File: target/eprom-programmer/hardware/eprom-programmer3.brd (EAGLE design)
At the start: 68.6 x 61 mm, 42 parts, among them IC2 27C08032P6, Q1 BC557, Q2 BC557, Q3 BC557

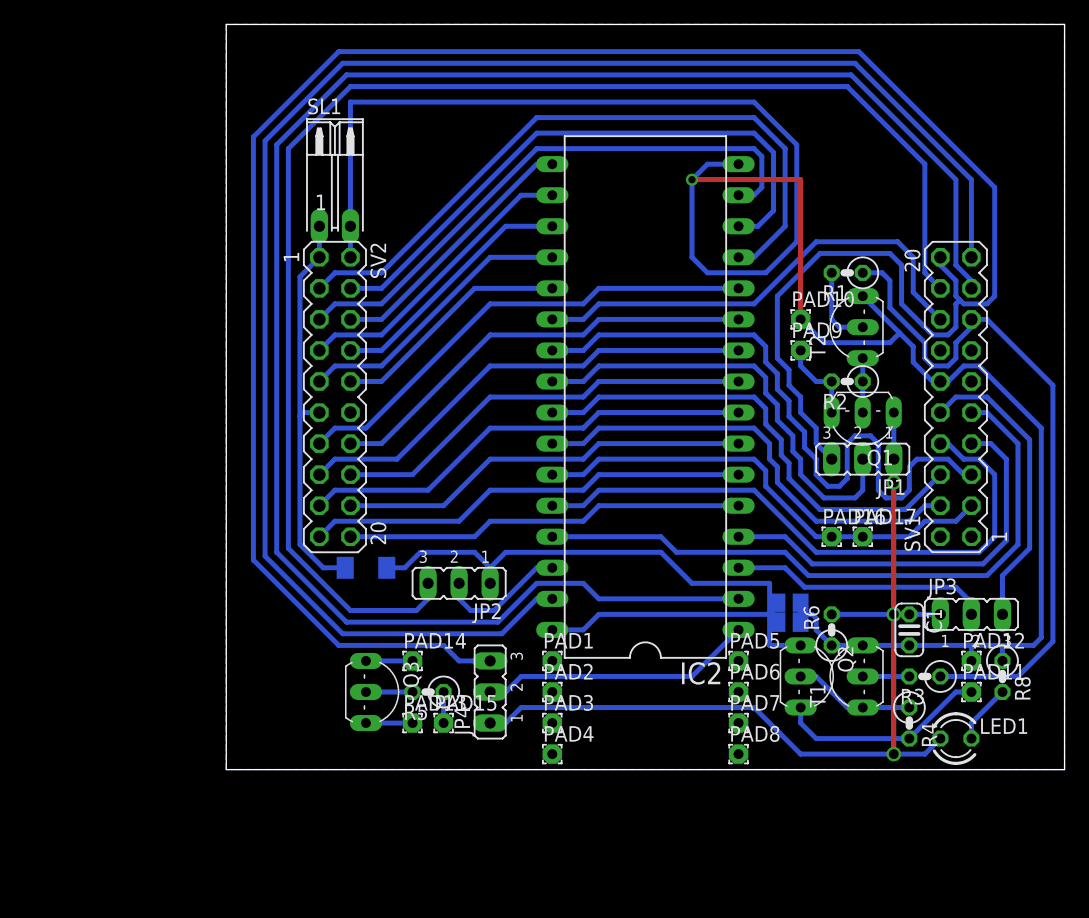
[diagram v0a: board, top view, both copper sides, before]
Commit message: eprom-programmer: hardware
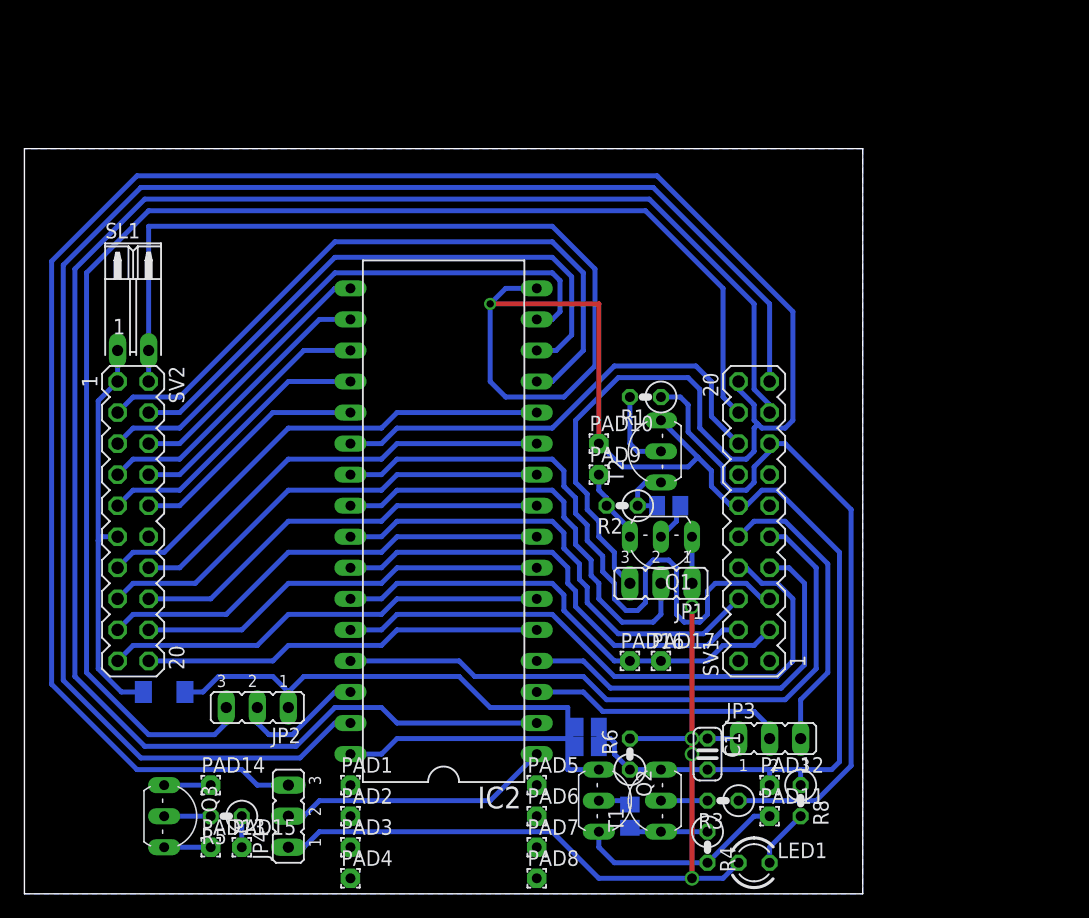
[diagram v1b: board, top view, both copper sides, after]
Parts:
- added R10, R9: 5k1, rcl:M0805
- moved R2 21.0 mm to (48.9, 31.8)
- moved PAD6 19.4 mm to (41.9, 6.35)
- moved D1 19.4 mm to (11.4, 16.5)
- moved JP4 19.4 mm to (21.6, 6.35)
- moved LED1 19.4 mm to (59.7, 2.54)
- moved PAD16 19.4 mm to (49.5, 19.1)
- moved PAD5 19.4 mm to (41.9, 8.89)
- moved PAD7 19.4 mm to (41.9, 3.81)
- moved PAD8 19.4 mm to (41.9, 1.27)
- moved Q3 19.4 mm to (12.7, 6.35)
- moved R1 19.4 mm to (50.8, 40.6)
- moved R5 19.4 mm to (16.5, 6.35)
- moved R6 19.4 mm to (49.5, 11.4)
- moved R8 19.4 mm to (63.5, 7.62)
- moved SV1 19.4 mm to (59.7, 30.5)
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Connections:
- new net N$11: Q1.B, R9.1
- new net N$14: Q2.B, R10.1
- net N$2: now also R10.2; no longer Q2.B
- net N$4: now also R9.2; no longer Q1.B
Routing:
- net N$2: track 9.94 -> 6.67 mm
- net N$11: track 0.00 -> 3.20 mm
- net N$14: track 0.00 -> 2.86 mm
- net VPROG_IN: track 6.88 -> 6.13 mm
- net N$4: track 4.45 -> 5.03 mm
- net VPP: vias 3 -> 4
